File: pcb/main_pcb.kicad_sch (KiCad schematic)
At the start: 36 parts, among them J1 Conn_01x06_Socket, J2 Conn_01x10_Pin, J3 Conn_01x06_Pin, J4 USB_C_Receptacle_USB2.0, Q1 Si2323DS, SW1 SW_Push, SW2 SW_Push, SW3 SW_Push, U1 ESP32-H2-MINI-1, U2 LM5165Y

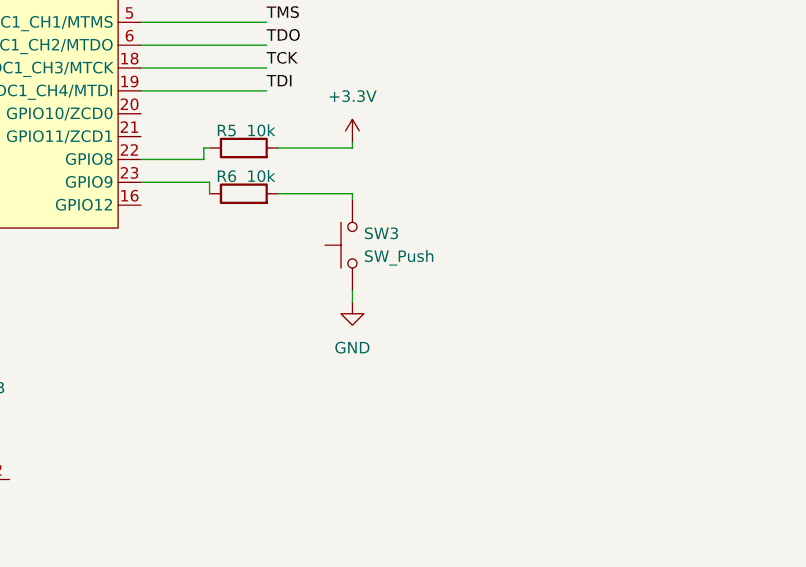
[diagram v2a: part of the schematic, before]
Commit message: Add capacitor to boot switch
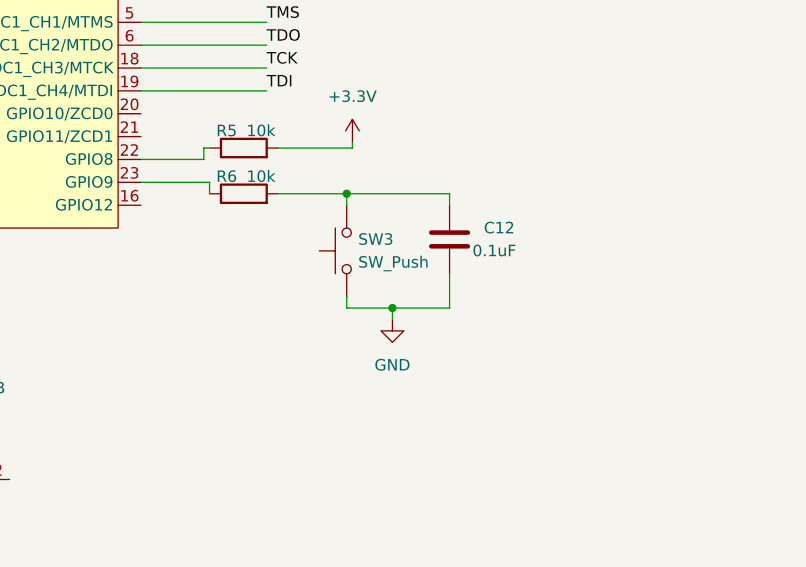
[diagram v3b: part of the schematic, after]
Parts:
- added C12: 0.1uF, Capacitor_SMD:C_1206_3216Metric_Pad1.33x1.80mm_HandSolder, symbol Device:C
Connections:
- net GND: now also C12.2
- net at R6.2, SW3.2: now also C12.1
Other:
- moved on the sheet: SW3
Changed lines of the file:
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@@
   (junction (at 55.88 83.82) (diameter 0) (color 0 0 0 0)
   )
+  (junction (at 215.9 99.06) (diameter 0) (color 0 0 0 0)
+  )
   (junction (at 48.26 78.74) (diameter 0) (color 0 0 0 0)
   )
@@
   )
   (junction (at 165.735 162.56) (diameter 0) (color 0 0 0 0)
+  )
+  (junction (at 220.98 111.76) (diameter 0) (color 0 0 0 0)
   )
   (junction (at 192.405 187.96) (diameter 0) (color 0 0 0 0)
@@
     (stroke (width 0) (type default))
   )
+  (wire (pts (xy 220.98 111.76) (xy 215.9 111.76))
+    (stroke (width 0) (type default))
+  )
   (wire (pts (xy 155.575 182.88) (xy 167.005 182.88))
     (stroke (width 0) (type default))
@@
     (stroke (width 0) (type default))
   )
-  (wire (pts (xy 216.535 99.695) (xy 216.535 99.06))
+  (wire (pts (xy 215.9 100.33) (xy 215.9 99.06))
     (stroke (width 0) (type default))
   )
@@
     (stroke (width 0) (type default))
   )
-  (wire (pts (xy 216.535 109.855) (xy 216.535 111.125))
+  (wire (pts (xy 215.9 110.49) (xy 215.9 111.76))
     (stroke (width 0) (type default))
   )
@@
     (stroke (width 0) (type default))
   )
+  (wire (pts (xy 227.33 100.33) (xy 227.33 99.06))
+    (stroke (width 0) (type default))
+  )
   (wire (pts (xy 48.26 71.12) (xy 57.15 71.12))
     (stroke (width 0) (type default))
@@
     (stroke (width 0) (type default))
   )
-  (wire (pts (xy 216.535 99.06) (xy 208.28 99.06))
+  (wire (pts (xy 208.28 99.06) (xy 215.9 99.06))
     (stroke (width 0) (type default))
   )
@@
     (stroke (width 0) (type default))
   )
+  (wire (pts (xy 227.33 107.95) (xy 227.33 111.76))
+    (stroke (width 0) (type default))
+  )
   (wire (pts (xy 158.115 163.83) (xy 158.115 162.56))
     (stroke (width 0) (type default))
@@
     (stroke (width 0) (type default))
   )
+  (wire (pts (xy 227.33 111.76) (xy 220.98 111.76))
+    (stroke (width 0) (type default))
+  )
   (wire (pts (xy 105.41 219.71) (xy 113.03 219.71))
     (stroke (width 0) (type default))
@@
   )
   (wire (pts (xy 229.235 196.85) (xy 229.235 199.39))
+    (stroke (width 0) (type default))
+  )
+  (wire (pts (xy 220.98 111.76) (xy 220.98 113.03))
+    (stroke (width 0) (type default))
+  )
+  (wire (pts (xy 215.9 99.06) (xy 227.33 99.06))
     (stroke (width 0) (type default))
   )
@@
     )
   )
-  (symbol (lib_id "Switch:SW_Push") (at 216.535 104.775 90) (unit 1)
-    (in_bom yes) (on_board yes) (dnp no) (fields_autoplaced)
-    (property "Reference" "SW3" (at 217.805 103.505 90)
+  (symbol (lib_id "Switch:SW_Push") (at 215.9 105.41 90) (unit 1)
+    (in_bom yes) (on_board yes) (dnp no) (fields_autoplaced)
+    (property "Reference" "SW3" (at 217.17 104.14 90)
       (effects (font (size 1.27 1.27)) (justify right))
     )
-    (property "Value" "SW_Push" (at 217.805 106.045 90)
+    (property "Value" "SW_Push" (at 217.17 106.68 90)
       (effects (font (size 1.27 1.27)) (justify right))
     )
-    (property "Footprint" "Button_Switch_SMD:SW_SPST_PTS645" (at 211.455 104.775 0)
-      (effects (font (size 1.27 1.27)) hide)
-    )
-    (property "Datasheet" "~" (at 211.455 104.775 0)
+    (property "Footprint" "Button_Switch_SMD:SW_SPST_PTS645" (at 210.82 105.41 0)
+      (effects (font (size 1.27 1.27)) hide)
+    )
+    (property "Datasheet" "~" (at 210.82 105.41 0)
       (effects (font (size 1.27 1.27)) hide)
     )
@@
     )
   )
-  (symbol (lib_id "power:GND") (at 216.535 111.125 0) (unit 1)
-    (in_bom yes) (on_board yes) (dnp no) (fields_autoplaced)
-    (property "Reference" "#PWR026" (at 216.535 117.475 0)
-      (effects (font (size 1.27 1.27)) hide)
-    )
-    (property "Value" "GND" (at 216.535 116.205 0)
-      (effects (font (size 1.27 1.27)))
-    )
-    (property "Footprint" "" (at 216.535 111.125 0)
-      (effects (font (size 1.27 1.27)) hide)
-    )
-    (property "Datasheet" "" (at 216.535 111.125 0)
+  (symbol (lib_id "power:GND") (at 220.98 113.03 0) (unit 1)
+    (in_bom yes) (on_board yes) (dnp no) (fields_autoplaced)
+    (property "Reference" "#PWR026" (at 220.98 119.38 0)
+      (effects (font (size 1.27 1.27)) hide)
+    )
+    (property "Value" "GND" (at 220.98 118.11 0)
+      (effects (font (size 1.27 1.27)))
+    )
+    (property "Footprint" "" (at 220.98 113.03 0)
+      (effects (font (size 1.27 1.27)) hide)
+    )
+    (property "Datasheet" "" (at 220.98 113.03 0)
       (effects (font (size 1.27 1.27)) hide)
     )
@@
         )
       )
+    )
+  )
+  (symbol (lib_id "Device:C") (at 227.33 104.14 0) (unit 1)
+    (in_bom yes) (on_board yes) (dnp no)
+    (property "Reference" "C12" (at 231.14 102.87 0)
+      (effects (font (size 1.27 1.27)) (justify left))
+    )
+    (property "Value" "0.1uF" (at 229.87 105.41 0)
+      (effects (font (size 1.27 1.27)) (justify left))
+    )
+    (property "Footprint" "Capacitor_SMD:C_1206_3216Metric_Pad1.33x1.80mm_HandSolder" (at 228.2952 107.95 0)
+      (effects (font (size 1.27 1.27)) hide)
+    )
+    (property "Datasheet" "~" (at 227.33 104.14 0)
+      (effects (font (size 1.27 1.27)) hide)
+    )
+    (pin "2")
+    (pin "1")
+    (instances
+      (project "main_pcb"
+        (path "/6204b7c2-8814-41ee-9243-5078f55f08d4"
+          (reference "C12") (unit 1)
+        )
+      )

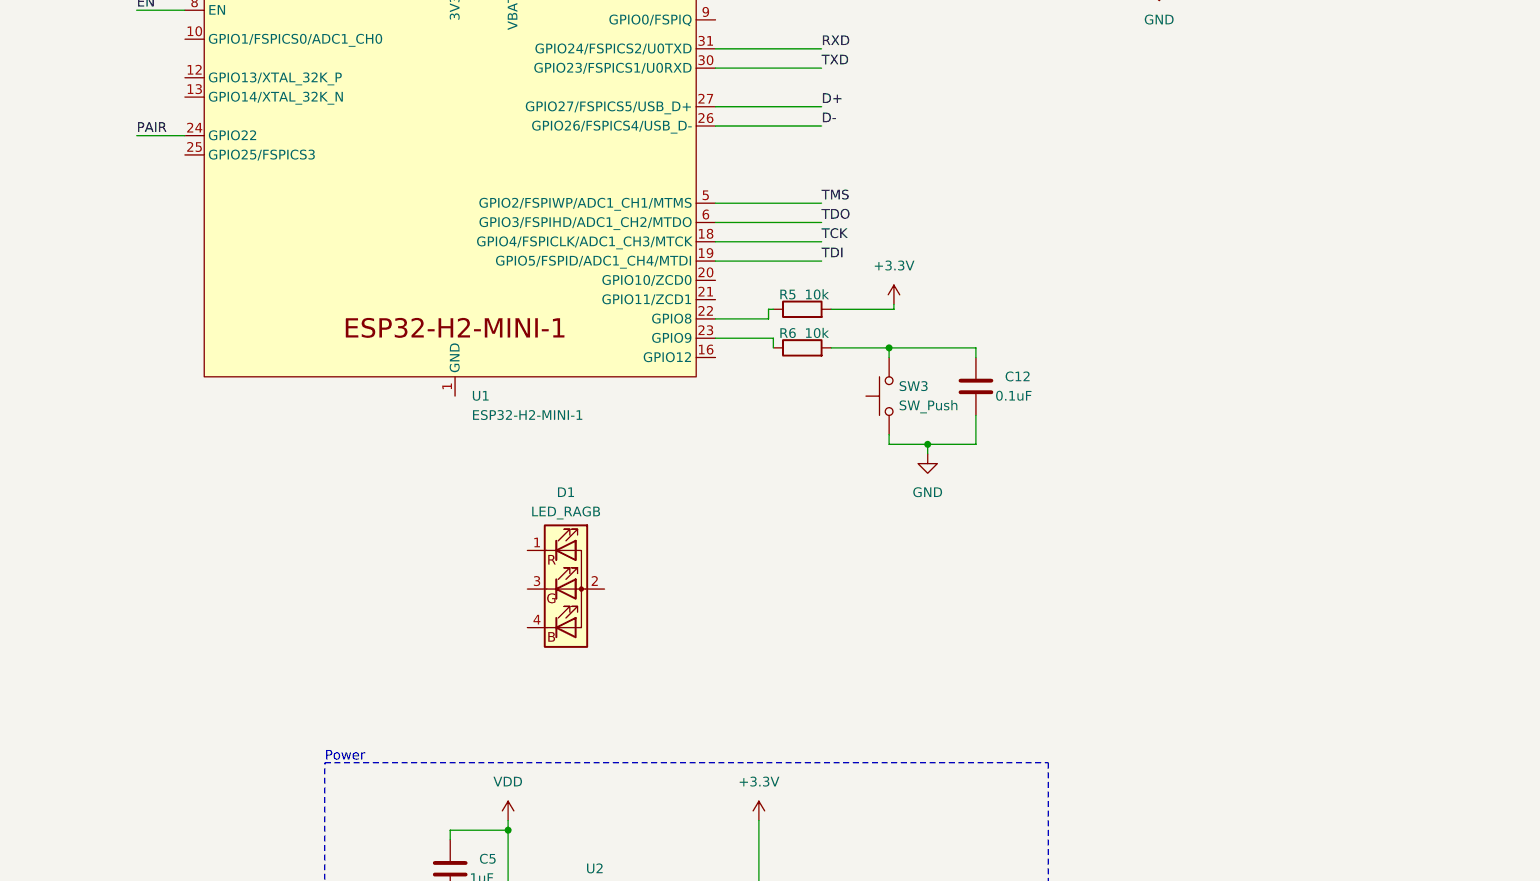
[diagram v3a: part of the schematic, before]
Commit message: Add status LED circuit
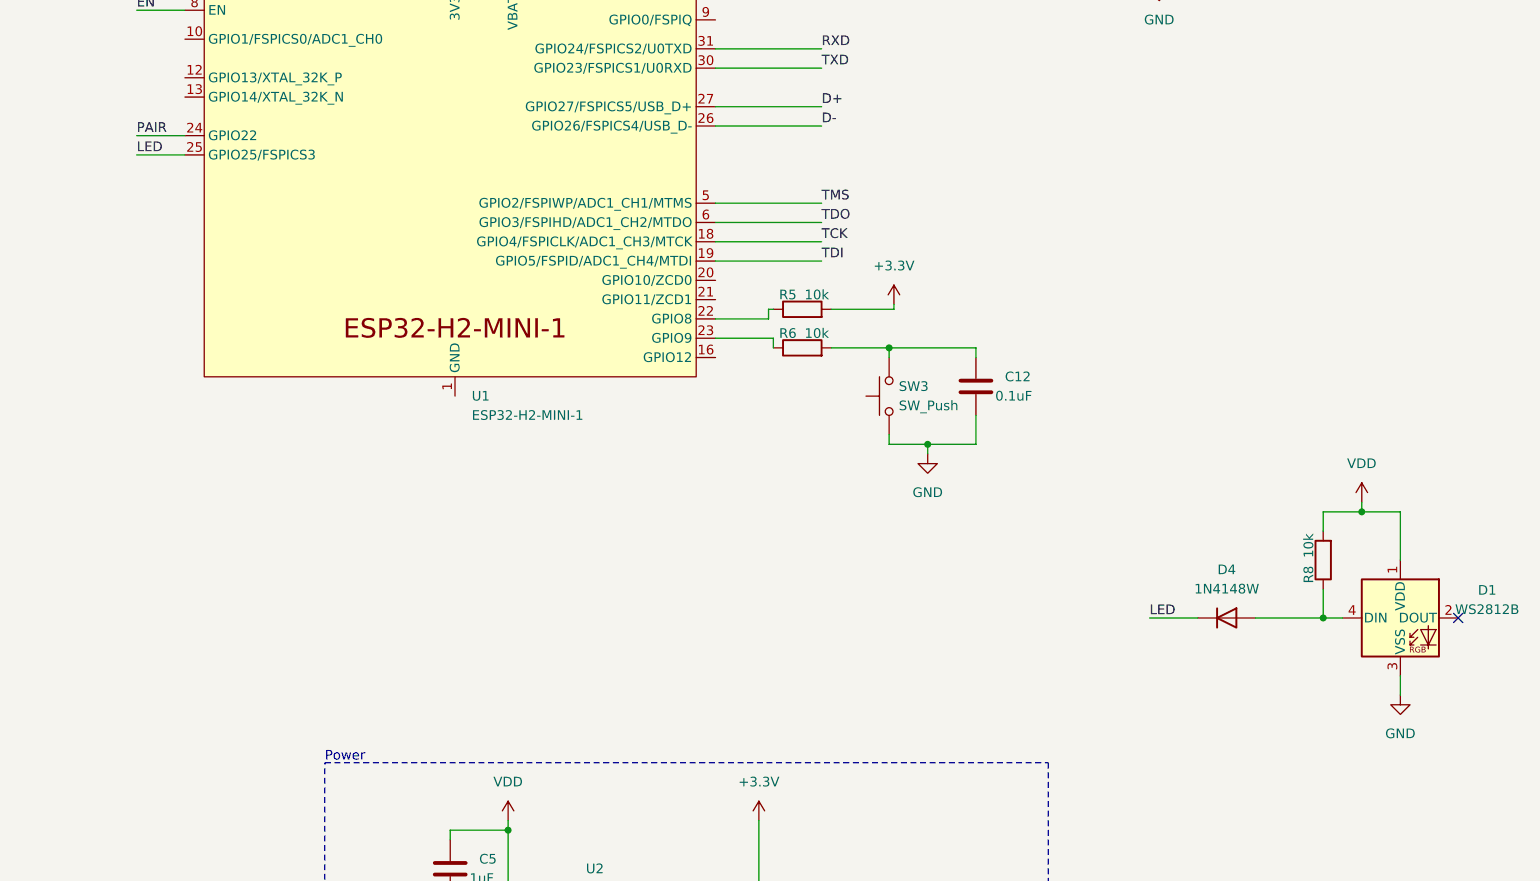
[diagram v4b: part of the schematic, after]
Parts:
- removed D1: LED_RAGB, LED_SMD:LED_RGB_1210, symbol Device:LED_RAGB
- added D1: WS2812B, LED_SMD:LED_WS2812B_PLCC4_5.0x5.0mm_P3.2mm, symbol LED:WS2812B
- added D4: 1N4148W, Diode_SMD:D_SOD-123, symbol Diode:1N4148W
- added R8: 10k, Resistor_SMD:R_1206_3216Metric_Pad1.30x1.75mm_HandSolder, symbol Device:R
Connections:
- net GND: now also D1.3 (VSS)
- net VDD: now also D1.1 (VDD), R8.2
- net LED: now reaches U1.25 (GPIO25/FSPICS3)
- net LED: now also D4.1 (K)
- new net: D1.4 (DIN), D4.2 (A), R8.1
- no-connect marks 8 -> 9
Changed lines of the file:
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@@
   (junction (at 69.215 73.66) (diameter 0) (color 0 0 0 0)
   )
+  (junction (at 273.05 134.62) (diameter 0) (color 0 0 0 0)
+  )
   (junction (at 113.03 219.71) (diameter 0) (color 0 0 0 0)
   )
@@
   )
   (junction (at 198.755 180.34) (diameter 0) (color 0 0 0 0)
+  )
+  (junction (at 278.13 120.65) (diameter 0) (color 0 0 0 0)
   )
   (junction (at 68.58 63.5) (diameter 0) (color 0 0 0 0)
@@
   (no_connect (at 82.55 248.92))
   (no_connect (at 29.845 259.715))
+  (no_connect (at 290.83 134.62))
   (no_connect (at 82.55 251.46))
   (no_connect (at 33.02 194.31))
@@
     (stroke (width 0) (type default))
   )
+  (wire (pts (xy 275.59 134.62) (xy 273.05 134.62))
+    (stroke (width 0) (type default))
+  )
   (wire (pts (xy 248.92 49.53) (xy 251.46 49.53))
     (stroke (width 0) (type default))
@@
     (stroke (width 0) (type default))
   )
+  (wire (pts (xy 250.19 134.62) (xy 256.54 134.62))
+    (stroke (width 0) (type default))
+  )
   (wire (pts (xy 172.72 38.1) (xy 172.72 40.64))
     (stroke (width 0) (type default))
   )
+  (wire (pts (xy 273.05 120.65) (xy 278.13 120.65))
+    (stroke (width 0) (type default))
+  )
   (wire (pts (xy 33.02 199.39) (xy 45.72 199.39))
     (stroke (width 0) (type default))
@@
     (stroke (width 0) (type default))
   )
+  (wire (pts (xy 278.13 119.38) (xy 278.13 120.65))
+    (stroke (width 0) (type default))
+  )
+  (wire (pts (xy 116.84 73.66) (xy 123.19 73.66))
+    (stroke (width 0) (type default))
+  )
+  (wire (pts (xy 283.21 120.65) (xy 283.21 127))
+    (stroke (width 0) (type default))
+  )
   (wire (pts (xy 167.005 177.8) (xy 165.735 177.8))
     (stroke (width 0) (type default))
@@
     (stroke (width 0) (type default))
   )
+  (wire (pts (xy 278.13 120.65) (xy 283.21 120.65))
+    (stroke (width 0) (type default))
+  )
   (wire (pts (xy 90.17 219.71) (xy 90.17 229.87))
     (stroke (width 0) (type default))
@@
     (stroke (width 0) (type default))
   )
+  (wire (pts (xy 273.05 123.19) (xy 273.05 120.65))
+    (stroke (width 0) (type default))
+  )
   (wire (pts (xy 202.565 196.85) (xy 202.565 199.39))
     (stroke (width 0) (type default))
@@
     (stroke (width 0) (type default))
   )
+  (wire (pts (xy 273.05 134.62) (xy 273.05 130.81))
+    (stroke (width 0) (type default))
+  )
   (wire (pts (xy 68.58 63.5) (xy 74.93 63.5))
     (stroke (width 0) (type default))
@@
     (stroke (width 0) (type default))
   )
+  (wire (pts (xy 264.16 134.62) (xy 273.05 134.62))
+    (stroke (width 0) (type default))
+  )
   (wire (pts (xy 227.33 107.95) (xy 227.33 111.76))
     (stroke (width 0) (type default))
@@
   )
   (wire (pts (xy 82.55 254) (xy 90.17 254))
+    (stroke (width 0) (type default))
+  )
+  (wire (pts (xy 283.21 142.24) (xy 283.21 144.78))
     (stroke (width 0) (type default))
   )
@@
     (effects (font (size 1.27 1.27)) (justify left bottom))
   )
+  (label "LED" (at 116.84 73.66 0) (fields_autoplaced)
+    (effects (font (size 1.27 1.27)) (justify left bottom))
+  )
   (label "TDI" (at 207.01 87.63 0) (fields_autoplaced)
     (effects (font (size 1.27 1.27)) (justify left bottom))
@@
   )
   (label "PAIR" (at 241.3 38.1 0) (fields_autoplaced)
+    (effects (font (size 1.27 1.27)) (justify left bottom))
+  )
+  (label "LED" (at 250.19 134.62 0) (fields_autoplaced)
     (effects (font (size 1.27 1.27)) (justify left bottom))
   )
@@
     )
   )
+  (symbol (lib_id "Device:R") (at 273.05 127 180) (unit 1)
+    (in_bom yes) (on_board yes) (dnp no)
+    (property "Reference" "R8" (at 271.145 128.905 90)
+      (effects (font (size 1.27 1.27)))
+    )
+    (property "Value" "10k" (at 271.145 125.095 90)
+      (effects (font (size 1.27 1.27)))
+    )
+    (property "Footprint" "Resistor_SMD:R_1206_3216Metric_Pad1.30x1.75mm_HandSolder" (at 274.828 127 90)
+      (effects (font (size 1.27 1.27)) hide)
+    )
+    (property "Datasheet" "~" (at 273.05 127 0)
+      (effects (font (size 1.27 1.27)) hide)
+    )
+    (pin "2")
+    (pin "1")
+    (instances
+      (project "main_pcb"
+        (path "/6204b7c2-8814-41ee-9243-5078f55f08d4"
+          (reference "R8") (unit 1)
+        )
+      )
+    )
+  )
+  (symbol (lib_id "LED:WS2812B") (at 283.21 134.62 0) (unit 1)
+    (in_bom yes) (on_board yes) (dnp no) (fields_autoplaced)
+    (property "Reference" "D1" (at 294.64 130.9721 0)
+      (effects (font (size 1.27 1.27)))
+    )
+    (property "Value" "WS2812B" (at 294.64 133.5121 0)
+      (effects (font (size 1.27 1.27)))
+    )
+    (property "Footprint" "LED_SMD:LED_WS2812B_PLCC4_5.0x5.0mm_P3.2mm" (at 284.48 142.24 0)
+      (effects (font (size 1.27 1.27)) (justify left top) hide)
+    )
+    (property "Datasheet" "https://cdn-shop.adafruit.com/datasheets/WS2812B.pdf" (at 285.75 144.145 0)
+      (effects (font (size 1.27 1.27)) (justify left top) hide)
+    )
+    (pin "3")
+    (pin "2")
+    (pin "1")
+    (pin "4")
+    (instances
+      (project "main_pcb"
+        (path "/6204b7c2-8814-41ee-9243-5078f55f08d4"
+          (reference "D1") (unit 1)
+        )
+      )
+    )
+  )
   (symbol (lib_id "power:GND") (at 158.115 173.99 0) (unit 1)
     (in_bom yes) (on_board yes) (dnp no) (fields_autoplaced)
@@
     )
   )
+  (symbol (lib_id "Diode:1N4148W") (at 260.35 134.62 0) (unit 1)
+    (in_bom yes) (on_board yes) (dnp no) (fields_autoplaced)
+    (property "Reference" "D4" (at 260.35 128.27 0)
+      (effects (font (size 1.27 1.27)))
+    )
+    (property "Value" "1N4148W" (at 260.35 130.81 0)
+      (effects (font (size 1.27 1.27)))
+    )
+    (property "Footprint" "Diode_SMD:D_SOD-123" (at 260.35 139.065 0)
+      (effects (font (size 1.27 1.27)) hide)
+    )
+    (property "Datasheet" "https://www.vishay.com/docs/85748/1n4148w.pdf" (at 260.35 134.62 0)
+      (effects (font (size 1.27 1.27)) hide)
+    )
+    (property "Sim.Device" "D" (at 260.35 134.62 0)
+      (effects (font (size 1.27 1.27)) hide)
+    )
+    (property "Sim.Pins" "1=K 2=A" (at 260.35 134.62 0)
+      (effects (font (size 1.27 1.27)) hide)
+    )
+    (pin "2")
+    (pin "1")
+    (instances
+      (project "main_pcb"
+        (path "/6204b7c2-8814-41ee-9243-5078f55f08d4"
+          (reference "D4") (unit 1)
+        )
+      )
+    )
+  )
   (symbol (lib_id "power:GND") (at 101.6 238.76 0) (unit 1)
     (in_bom yes) (on_board yes) (dnp no)
@@
     )
   )
+  (symbol (lib_id "power:VDD") (at 278.13 119.38 0) (unit 1)
+    (in_bom yes) (on_board yes) (dnp no) (fields_autoplaced)
+    (property "Reference" "#PWR033" (at 278.13 123.19 0)
+      (effects (font (size 1.27 1.27)) hide)
+    )
+    (property "Value" "VDD" (at 278.13 114.3 0)
+      (effects (font (size 1.27 1.27)))
+    )
+    (property "Footprint" "" (at 278.13 119.38 0)
+      (effects (font (size 1.27 1.27)) hide)
+    )
+    (property "Datasheet" "" (at 278.13 119.38 0)
+      (effects (font (size 1.27 1.27)) hide)
+    )
+    (pin "1")
+    (instances
+      (project "main_pcb"
+        (path "/6204b7c2-8814-41ee-9243-5078f55f08d4"
+          (reference "#PWR033") (unit 1)
+        )
+      )
+    )
+  )
   (symbol (lib_id "power:GND") (at 220.98 113.03 0) (unit 1)
     (in_bom yes) (on_board yes) (dnp no) (fields_autoplaced)
@@
         (path "/6204b7c2-8814-41ee-9243-5078f55f08d4"
           (reference "#PWR012") (unit 1)
-        )
-      )
-    )
-  )
-  (symbol (lib_id "Device:LED_RAGB") (at 173.355 130.81 0) (unit 1)
-    (in_bom yes) (on_board yes) (dnp no) (fields_autoplaced)
-    (property "Reference" "D1" (at 173.355 118.11 0)
-      (effects (font (size 1.27 1.27)))
-    )
-    (property "Value" "LED_RAGB" (at 173.355 120.65 0)
-      (effects (font (size 1.27 1.27)))
-    )
-    (property "Footprint" "LED_SMD:LED_RGB_1210" (at 173.355 132.08 0)
-      (effects (font (size 1.27 1.27)) hide)
-    )
-    (property "Datasheet" "~" (at 173.355 132.08 0)
-      (effects (font (size 1.27 1.27)) hide)
-    )
-    (pin "2")
-    (pin "1")
-    (pin "3")
-    (pin "4")
-    (instances
-      (project "main_pcb"
-        (path "/6204b7c2-8814-41ee-9243-5078f55f08d4"
-          (reference "D1") (unit 1)
         )
       )
@@
         )
       )
+    )
+  )
+  (symbol (lib_id "power:GND") (at 283.21 144.78 0) (unit 1)
+    (in_bom yes) (on_board yes) (dnp no) (fields_autoplaced)
+    (property "Reference" "#PWR034" (at 283.21 151.13 0)
+      (effects (font (size 1.27 1.27)) hide)
+    )
+    (property "Value" "GND" (at 283.21 149.86 0)
+      (effects (font (size 1.27 1.27)))
+    )
+    (property "Footprint" "" (at 283.21 144.78 0)
+      (effects (font (size 1.27 1.27)) hide)
+    )
+    (property "Datasheet" "" (at 283.21 144.78 0)
+      (effects (font (size 1.27 1.27)) hide)
+    )
+    (pin "1")
+    (instances
+      (project "main_pcb"
+        (path "/6204b7c2-8814-41ee-9243-5078f55f08d4"
+          (reference "#PWR034") (unit 1)
+        )
+      )
